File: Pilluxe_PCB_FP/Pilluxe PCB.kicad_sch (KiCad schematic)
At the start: 35 parts, among them J1 USB_C_Receptacle_USB2.0_16P, U1 ESP32-S3-MINI-1, U2 AP2112K-3.3, U3 MCP73831-2-OT, U4 LSM6DSL

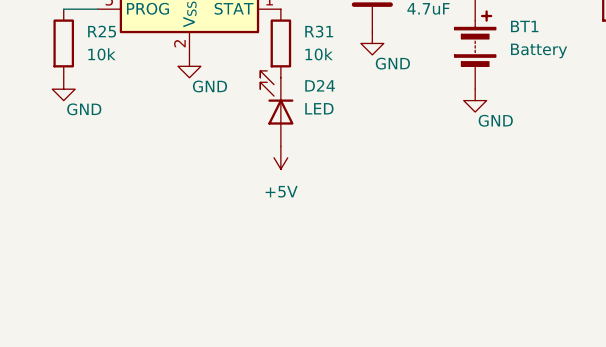
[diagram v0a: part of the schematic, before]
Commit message: Adding battery to the schematic attached to NOTHING
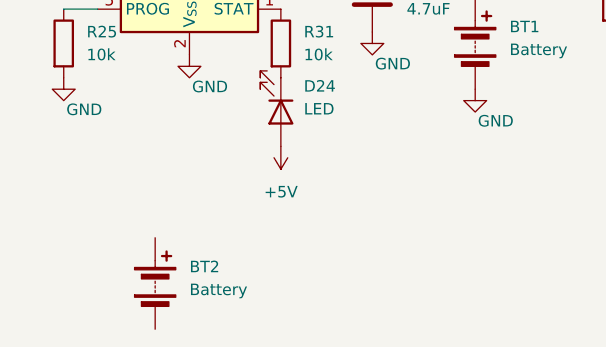
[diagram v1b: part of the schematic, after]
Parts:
- added BT2: Battery, symbol Device:Battery
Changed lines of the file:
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@@
+	)
+	(symbol
+		(lib_id "Device:Battery")
+		(at 27.94 166.37 0)
+		(unit 1)
+		(body_style 1)
+		(exclude_from_sim no)
+		(in_bom yes)
+		(on_board yes)
+		(in_pos_files yes)
+		(dnp no)
+		(fields_autoplaced yes)
+		(property "Reference" "BT2"
+			(at 31.75 164.5284 0)
+			(show_name no)
+			(do_not_autoplace no)
+			(effects
+				(font
+					(size 1.27 1.27)
+				)
+				(justify left)
+			)
+		)
+		(property "Value" "Battery"
+			(at 31.75 167.0684 0)
+			(show_name no)
+			(do_not_autoplace no)
+			(effects
+				(font
+					(size 1.27 1.27)
+				)
+				(justify left)
+			)
+		)
+		(property "Footprint" ""
+			(at 27.94 164.846 90)
+			(hide yes)
+			(show_name no)
+			(do_not_autoplace no)
+			(effects
+				(font
+					(size 1.27 1.27)
+				)
+			)
+		)
+		(property "Datasheet" ""
+			(at 27.94 164.846 90)
+			(hide yes)
+			(show_name no)
+			(do_not_autoplace no)
+			(effects
+				(font
+					(size 1.27 1.27)
+				)
+			)
+		)
+		(property "Description" "Multiple-cell battery"
+			(at 27.94 166.37 0)
+			(hide yes)
+			(show_name no)
+			(do_not_autoplace no)
+			(effects
+				(font
+					(size 1.27 1.27)
+				)
+			)
+		)
+		(property "Sim.Device" "V"
+			(at 27.94 166.37 0)
+			(hide yes)
+			(show_name no)
+			(do_not_autoplace no)
+			(effects
+				(font
+					(size 1.27 1.27)
+				)
+			)
+		)
+		(property "Sim.Type" "DC"
+			(at 27.94 166.37 0)
+			(hide yes)
+			(show_name no)
+			(do_not_autoplace no)
+			(effects
+				(font
+					(size 1.27 1.27)
+				)
+			)
+		)
+		(property "Sim.Pins" "1=+ 2=-"
+			(at 27.94 166.37 0)
+			(hide yes)
+			(show_name no)
+			(do_not_autoplace no)
+			(effects
+				(font
+					(size 1.27 1.27)
+				)
+			)
+		)
+		(pin "2"
+		)
+		(pin "1"
+		)
+		(instances
+			(project "Pilluxe PCB"
+				(path "/dda724c3-02bd-4c4c-9437-672e1c9e0281"
+					(reference "BT2")
+					(unit 1)
+				)
+			)
+		)
 	)
 	(symbol

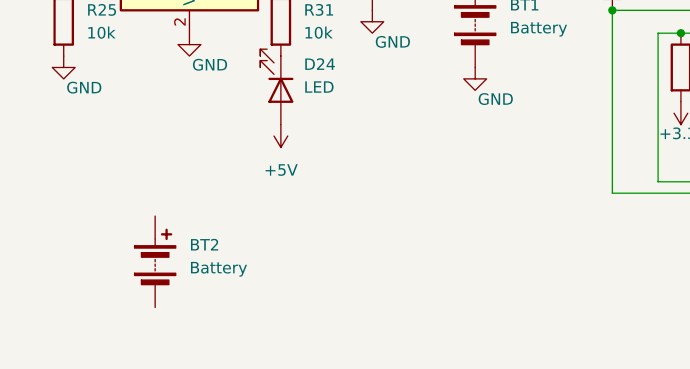
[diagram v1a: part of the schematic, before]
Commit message: adding capacitor
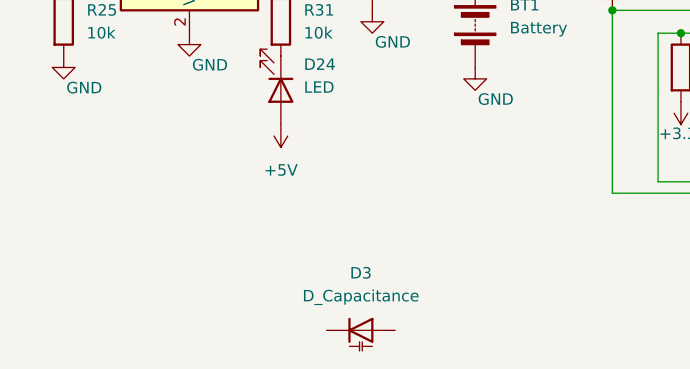
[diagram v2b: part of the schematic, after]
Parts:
- removed BT2: Battery, symbol Device:Battery
- added D3: D_Capacitance, symbol Device:D_Capacitance
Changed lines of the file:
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@@
-	)
-	(symbol
-		(lib_id "Device:Battery")
-		(at 27.94 166.37 0)
-		(unit 1)
-		(body_style 1)
-		(exclude_from_sim no)
-		(in_bom yes)
-		(on_board yes)
-		(in_pos_files yes)
-		(dnp no)
-		(fields_autoplaced yes)
-		(property "Reference" "BT2"
-			(at 31.75 164.5284 0)
-			(show_name no)
-			(do_not_autoplace no)
-			(effects
-				(font
-					(size 1.27 1.27)
-				)
-				(justify left)
-			)
-		)
-		(property "Value" "Battery"
-			(at 31.75 167.0684 0)
-			(show_name no)
-			(do_not_autoplace no)
-			(effects
-				(font
-					(size 1.27 1.27)
-				)
-				(justify left)
-			)
-		)
-		(property "Footprint" ""
-			(at 27.94 164.846 90)
-			(hide yes)
-			(show_name no)
-			(do_not_autoplace no)
-			(effects
-				(font
-					(size 1.27 1.27)
-				)
-			)
-		)
-		(property "Datasheet" ""
-			(at 27.94 164.846 90)
-			(hide yes)
-			(show_name no)
-			(do_not_autoplace no)
-			(effects
-				(font
-					(size 1.27 1.27)
-				)
-			)
-		)
-		(property "Description" "Multiple-cell battery"
-			(at 27.94 166.37 0)
-			(hide yes)
-			(show_name no)
-			(do_not_autoplace no)
-			(effects
-				(font
-					(size 1.27 1.27)
-				)
-			)
-		)
-		(property "Sim.Device" "V"
-			(at 27.94 166.37 0)
-			(hide yes)
-			(show_name no)
-			(do_not_autoplace no)
-			(effects
-				(font
-					(size 1.27 1.27)
-				)
-			)
-		)
-		(property "Sim.Type" "DC"
-			(at 27.94 166.37 0)
-			(hide yes)
-			(show_name no)
-			(do_not_autoplace no)
-			(effects
-				(font
-					(size 1.27 1.27)
-				)
-			)
-		)
-		(property "Sim.Pins" "1=+ 2=-"
-			(at 27.94 166.37 0)
-			(hide yes)
-			(show_name no)
-			(do_not_autoplace no)
-			(effects
-				(font
-					(size 1.27 1.27)
-				)
-			)
-		)
-		(pin "2"
-		)
-		(pin "1"
-		)
-		(instances
-			(project "Pilluxe PCB"
-				(path "/dda724c3-02bd-4c4c-9437-672e1c9e0281"
-					(reference "BT2")
-					(unit 1)
-				)
-			)
-		)
 	)
 	(symbol
@@
 					(unit 1)
 				)
+			)
+		)
+	)
+	(symbol
+		(lib_id "Device:D_Capacitance")
+		(at 50.8 173.99 0)
+		(unit 1)
+		(body_style 1)
+		(exclude_from_sim no)
+		(in_bom yes)
+		(on_board yes)
+		(in_pos_files yes)
+		(dnp no)
+		(fields_autoplaced yes)
+		(property "Reference" "D3"
+			(at 50.8 167.64 0)
+			(show_name no)
+			(do_not_autoplace no)
+			(effects
+				(font
+					(size 1.27 1.27)
+				)
+			)
+		)
+		(property "Value" "D_Capacitance"
+			(at 50.8 170.18 0)
+			(show_name no)
+			(do_not_autoplace no)
+			(effects
+				(font
+					(size 1.27 1.27)
+				)
+			)
+		)
+		(property "Footprint" ""
+			(at 50.8 173.99 0)
+			(hide yes)
+			(show_name no)
+			(do_not_autoplace no)
+			(effects
+				(font
+					(size 1.27 1.27)
+				)
+			)
+		)
+		(property "Datasheet" ""
+			(at 50.8 173.99 0)
+			(hide yes)
+			(show_name no)
+			(do_not_autoplace no)
+			(effects
+				(font
+					(size 1.27 1.27)
+				)
+			)
+		)
+		(property "Description" "Variable capacitance diode"
+			(at 50.8 173.99 0)
+			(hide yes)
+			(show_name no)
+			(do_not_autoplace no)
+			(effects
+				(font
+					(size 1.27 1.27)
+				)
+			)
+		)
+		(pin "2"
+		)
+		(pin "1"
+		)
+		(instances
+			(project "Pilluxe PCB"
+				(path "/dda724c3-02bd-4c4c-9437-672e1c9e0281"
+					(reference "D3")
+					(unit 1)
+				)
